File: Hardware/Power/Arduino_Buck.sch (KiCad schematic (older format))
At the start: 9 parts, among them Q3 2N7000, Q4 PJM2301PSA-S

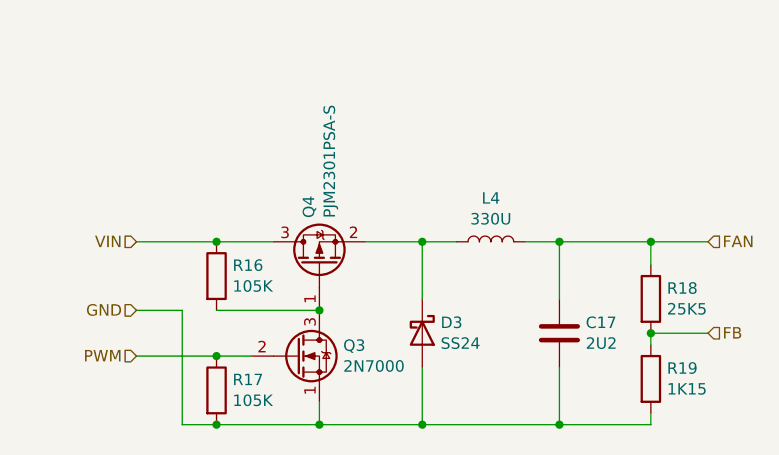
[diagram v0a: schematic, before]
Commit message: Moved MCU Power Supply to Logic Board
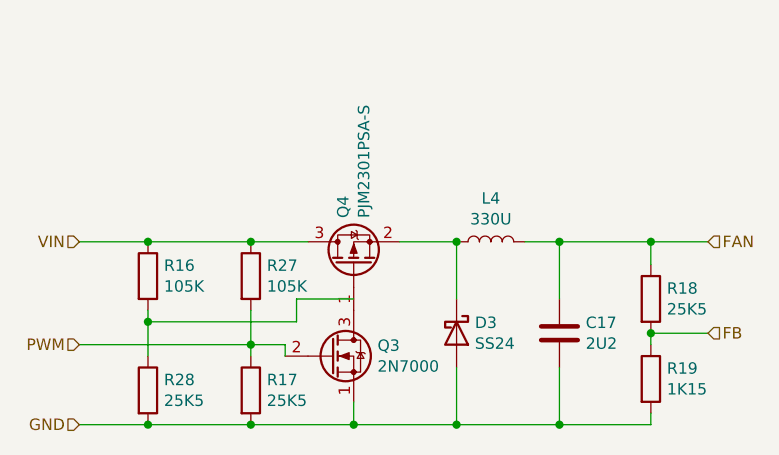
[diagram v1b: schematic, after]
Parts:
- added R27: 105K, Resistor_SMD:R_0603_1608Metric_Pad1.05x0.95mm_HandSolder, symbol Device:R
- added R28: 25K5, Resistor_SMD:R_0603_1608Metric_Pad1.05x0.95mm_HandSolder, symbol Device:R
- D3: Arrow Part Number (none) -> C181203; Mouser Part Number C181203 -> (none)
- R17: value 105K -> 25K5; Manufacturer_Part_Number RC0603FR-07105KL -> RS-05K2552FT
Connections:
- wire segments 26 -> 32
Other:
- moved on the sheet: D3, Q3, Q4, R16, R17
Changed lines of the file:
@@
 Comment4 ""
 $EndDescr
-Text HLabel 4700 3600 0    50   Input ~ 0
+Text HLabel 4450 3600 0    50   Input ~ 0
 VIN
 Text HLabel 7200 3600 2    50   Input ~ 0
 FAN
-Text HLabel 4700 3900 0    50   Input ~ 0
+Text HLabel 4450 4400 0    50   Input ~ 0
 GND
 Text HLabel 7200 4000 2    50   Input ~ 0
 FB
-Text HLabel 4700 4100 0    50   Input ~ 0
-PWM
 $Comp
 L Transistor_FET:TSM2301ACX Q4
 U 1 1 5F8E71B4
-P 5500 3700
-F 0 "Q4" H 5704 3746 50  0000 L CNN
-F 1 "PJM2301PSA-S" H 5704 3655 50  0000 L CNN
-F 2 "Package_TO_SOT_SMD:SOT-23" H 5700 3625 50  0001 L CIN
-F 3 "https://www.taiwansemi.com/products/datasheet/TSM2301A_C15.pdf" H 5500 3700 50  0001 L CNN
-F 4 "PJM2301PSA-S" H 5500 3700 50  0001 C CNN "Manufacturer_Part_Number"
-	1    5500 3700
+P 5650 3700
+F 0 "Q4" H 5854 3746 50  0000 L CNN
+F 1 "PJM2301PSA-S" H 5854 3655 50  0000 L CNN
+F 2 "Package_TO_SOT_SMD:SOT-23" H 5850 3625 50  0001 L CIN
+F 3 "https://www.taiwansemi.com/products/datasheet/TSM2301A_C15.pdf" H 5650 3700 50  0001 L CNN
+F 4 "PJM2301PSA-S" H 5650 3700 50  0001 C CNN "Manufacturer_Part_Number"
+	1    5650 3700
 	0    -1   -1   0
 $EndComp
@@
 L Device:D_Schottky D3
 U 1 1 5F8E9922
-P 5950 4000
-F 0 "D3" V 5904 4080 50  0000 L CNN
-F 1 "SS24" V 5995 4080 50  0000 L CNN
-F 2 "ArduinoLamp:D_SMA_Handsoldering_Shortened" H 5950 4000 50  0001 C CNN
-F 3 "~" H 5950 4000 50  0001 C CNN
-F 4 "C181203" H 5950 4000 50  0001 C CNN "Mouser Part Number"
-	1    5950 4000
+P 6100 4000
+F 0 "D3" V 6054 4080 50  0000 L CNN
+F 1 "SS24" V 6145 4080 50  0000 L CNN
+F 2 "ArduinoLamp:D_SMA_Handsoldering_Shortened" H 6100 4000 50  0001 C CNN
+F 3 "~" H 6100 4000 50  0001 C CNN
+F 4 "" H 6100 4000 50  0001 C CNN "Mouser Part Number"
+F 5 "C181203" H 6100 4000 50  0001 C CNN "Arrow Part Number"
+	1    6100 4000
 	0    1    1    0
 $EndComp
@@
 Wire Wire Line
 	6950 4050 6950 4000
+Wire Wire Line
+	6950 4000 7200 4000
+Connection ~ 6950 4000
+$Comp
+L Device:R R17
+U 1 1 5F8F67F8
+P 5200 4250
+F 0 "R17" H 5270 4296 50  0000 L CNN
+F 1 "25K5" H 5270 4205 50  0000 L CNN
+F 2 "Resistor_SMD:R_0603_1608Metric_Pad1.05x0.95mm_HandSolder" V 5130 4250 50  0001 C CNN
+F 3 "~" H 5200 4250 50  0001 C CNN
+F 4 "RS-05K2552FT" H 5200 4250 50  0001 C CNN "Manufacturer_Part_Number"
+	1    5200 4250
+	1    0    0    -1
+$EndComp
+Wire Wire Line
+	5650 4400 5650 4300
+Wire Wire Line
+	6550 4150 6550 4400
+Wire Wire Line
+	6950 4350 6950 4400
+Wire Wire Line
+	6950 4400 6550 4400
+Connection ~ 6550 4400
+Wire Wire Line
+	6550 3850 6550 3600
+Wire Wire Line
+	6550 3600 6950 3600
+Wire Wire Line
+	6950 3600 6950 3700
+Connection ~ 6950 3600
+Wire Wire Line
+	6950 3600 7200 3600
+Wire Wire Line
+	6400 3600 6550 3600
+Connection ~ 6550 3600
+Wire Wire Line
+	6100 3600 6100 3850
+Wire Wire Line
+	6100 4150 6100 4400
+$Comp
+L Device:R R27
+U 1 1 5FAF10C0
+P 5200 3750
+F 0 "R27" H 5270 3796 50  0000 L CNN
+F 1 "105K" H 5270 3705 50  0000 L CNN
+F 2 "Resistor_SMD:R_0603_1608Metric_Pad1.05x0.95mm_HandSolder" V 5130 3750 50  0001 C CNN
+F 3 "~" H 5200 3750 50  0001 C CNN
+F 4 "RC0603FR-07105KL" H 5200 3750 50  0001 C CNN "Manufacturer_Part_Number"
+	1    5200 3750
+	1    0    0    -1
+$EndComp
+$Comp
+L Device:R R16
+U 1 1 5F8FA0B3
+P 4750 3750
+F 0 "R16" H 4820 3796 50  0000 L CNN
+F 1 "105K" H 4820 3705 50  0000 L CNN
+F 2 "Resistor_SMD:R_0603_1608Metric_Pad1.05x0.95mm_HandSolder" V 4680 3750 50  0001 C CNN
+F 3 "~" H 4750 3750 50  0001 C CNN
+F 4 "RC0603FR-07105KL" H 4750 3750 50  0001 C CNN "Manufacturer_Part_Number"
+	1    4750 3750
+	1    0    0    -1
+$EndComp
+Connection ~ 5650 4400
+Connection ~ 6100 3600
+Wire Wire Line
+	5850 3600 6100 3600
+Connection ~ 6100 4400
+Wire Wire Line
+	6100 4400 6550 4400
+Wire Wire Line
+	5650 4400 6100 4400
 $Comp
 L Transistor_FET:2N7000 Q3
 U 1 1 5F8F3832
-P 5400 4100
-F 0 "Q3" H 5604 4146 50  0000 L CNN
-F 1 "2N7000" H 5604 4055 50  0000 L CNN
-F 2 "Package_TO_SOT_THT:TO-92_Inline" H 5600 4025 50  0001 L CIN
-F 3 "https://www.fairchildsemi.com/datasheets/2N/2N7000.pdf" H 5400 4100 50  0001 L CNN
-F 4 "2N7000" H 5400 4100 50  0001 C CNN "Manufacturer_Part_Number"
-	1    5400 4100
-	1    0    0    -1
-$EndComp
-Wire Wire Line
-	6950 4000 7200 4000
-Connection ~ 6950 4000
-Wire Wire Line
-	4700 4100 5050 4100
-$Comp
-L Device:R R17
-U 1 1 5F8F67F8
-P 5050 4250
-F 0 "R17" H 5120 4296 50  0000 L CNN
-F 1 "105K" H 5120 4205 50  0000 L CNN
-F 2 "Resistor_SMD:R_0603_1608Metric_Pad1.05x0.95mm_HandSolder" V 4980 4250 50  0001 C CNN
-F 3 "~" H 5050 4250 50  0001 C CNN
-F 4 "RC0603FR-07105KL" H 5050 4250 50  0001 C CNN "Manufacturer_Part_Number"
-	1    5050 4250
-	1    0    0    -1
-$EndComp
-Wire Wire Line
-	4700 3900 4900 3900
-$Comp
-L Device:R R16
-U 1 1 5F8FA0B3
-P 5050 3750
-F 0 "R16" H 5120 3796 50  0000 L CNN
-F 1 "105K" H 5120 3705 50  0000 L CNN
-F 2 "Resistor_SMD:R_0603_1608Metric_Pad1.05x0.95mm_HandSolder" V 4980 3750 50  0001 C CNN
-F 3 "~" H 5050 3750 50  0001 C CNN
-F 4 "RC0603FR-07105KL" H 5050 3750 50  0001 C CNN "Manufacturer_Part_Number"
-	1    5050 3750
-	1    0    0    -1
-$EndComp
-Wire Wire Line
-	4900 3900 4900 4400
-Wire Wire Line
-	4900 4400 5050 4400
-Wire Wire Line
-	5500 4400 5500 4300
-Connection ~ 5500 4400
-Wire Wire Line
-	6550 4150 6550 4400
-Wire Wire Line
-	6950 4350 6950 4400
-Wire Wire Line
-	6950 4400 6550 4400
-Connection ~ 6550 4400
-Wire Wire Line
-	4700 3600 5050 3600
-Connection ~ 5050 3600
-Wire Wire Line
-	5050 3600 5300 3600
-Wire Wire Line
-	5050 3900 5500 3900
-Connection ~ 5500 3900
-Wire Wire Line
-	6550 3850 6550 3600
-Wire Wire Line
-	6550 3600 6950 3600
-Wire Wire Line
-	6950 3600 6950 3700
-Connection ~ 6950 3600
-Wire Wire Line
-	6950 3600 7200 3600
-Connection ~ 5050 4100
-Connection ~ 5050 4400
-Wire Wire Line
-	5050 4100 5200 4100
-Wire Wire Line
-	5050 4400 5500 4400
-Wire Wire Line
-	6400 3600 6550 3600
-Connection ~ 6550 3600
-Wire Wire Line
-	5500 4400 5950 4400
-Wire Wire Line
-	5700 3600 5950 3600
-Wire Wire Line
-	5950 3600 5950 3850
-Connection ~ 5950 3600
-Wire Wire Line
-	5950 3600 6100 3600
-Wire Wire Line
-	5950 4150 5950 4400
-Connection ~ 5950 4400
-Wire Wire Line
-	5950 4400 6550 4400
+P 5550 4100
+F 0 "Q3" H 5754 4146 50  0000 L CNN
+F 1 "2N7000" H 5754 4055 50  0000 L CNN
+F 2 "Package_TO_SOT_THT:TO-92_Inline" H 5750 4025 50  0001 L CIN
+F 3 "https://www.fairchildsemi.com/datasheets/2N/2N7000.pdf" H 5550 4100 50  0001 L CNN
+F 4 "2N7000" H 5550 4100 50  0001 C CNN "Manufacturer_Part_Number"
+	1    5550 4100
+	1    0    0    -1
+$EndComp
+Connection ~ 5200 3600
+Wire Wire Line
+	5200 4400 5650 4400
+Wire Wire Line
+	4450 3600 4750 3600
+Connection ~ 4750 3600
+Wire Wire Line
+	4750 3600 5200 3600
+Wire Wire Line
+	4750 3900 4750 3950
+Wire Wire Line
+	5200 3600 5450 3600
+Wire Wire Line
+	5650 3850 5400 3850
+Wire Wire Line
+	5400 3850 5400 3950
+Wire Wire Line
+	5400 3950 4750 3950
+Connection ~ 4750 3950
+Wire Wire Line
+	4750 3950 4750 4100
+Wire Wire Line
+	4450 4050 5200 4050
+Text HLabel 4450 4050 0    50   Input ~ 0
+PWM
+Connection ~ 5200 4050
+Wire Wire Line
+	5200 4050 5200 4100
+Wire Wire Line
+	5200 3900 5200 4050
+Wire Wire Line
+	5200 4050 5350 4050
+Wire Wire Line
+	5350 4050 5350 4100
+$Comp
+L Device:R R28
+U 1 1 5FB23D33
+P 4750 4250
+F 0 "R28" H 4820 4296 50  0000 L CNN
+F 1 "25K5" H 4820 4205 50  0000 L CNN
+F 2 "Resistor_SMD:R_0603_1608Metric_Pad1.05x0.95mm_HandSolder" V 4680 4250 50  0001 C CNN
+F 3 "~" H 4750 4250 50  0001 C CNN
+F 4 "RS-05K2552FT" H 4750 4250 50  0001 C CNN "Manufacturer_Part_Number"
+	1    4750 4250
+	1    0    0    -1
+$EndComp
+Wire Wire Line
+	4450 4400 4750 4400
+Wire Wire Line
+	4750 4400 5200 4400
+Connection ~ 4750 4400
+Connection ~ 5200 4400
 $EndSCHEMATC

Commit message: Removed Logic Board PSU from Power Board
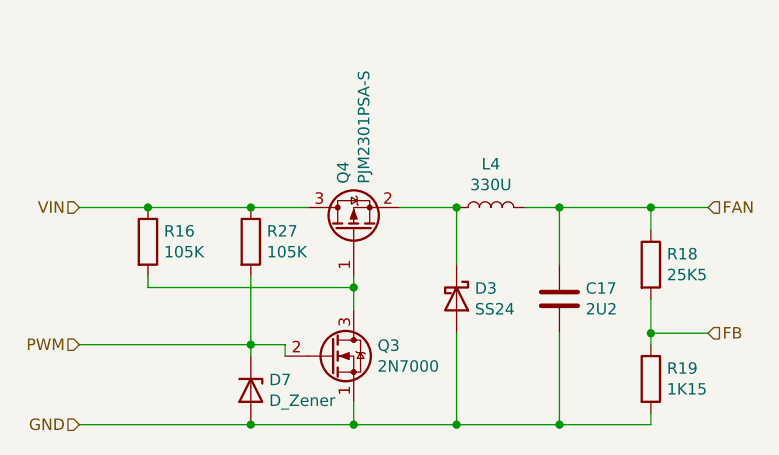
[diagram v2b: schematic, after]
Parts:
- removed R17, R28: 25K5, Resistor_SMD:R_0603_1608Metric_Pad1.05x0.95mm_HandSolder, symbol Device:R
- added D7: D_Zener, Diode_SMD:D_SOD-323_HandSoldering, symbol Device:D_Zener
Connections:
- wire segments 32 -> 31
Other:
- moved on the sheet: C17, D3, L4, Q4, R16, R18, R27
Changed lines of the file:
@@
 Comment4 ""
 $EndDescr
-Text HLabel 4450 3600 0    50   Input ~ 0
+Text HLabel 4450 3450 0    50   Input ~ 0
 VIN
-Text HLabel 7200 3600 2    50   Input ~ 0
+Text HLabel 7200 3450 2    50   Input ~ 0
 FAN
 Text HLabel 4450 4400 0    50   Input ~ 0
@@
 FB
 $Comp
-L Transistor_FET:TSM2301ACX Q4
-U 1 1 5F8E71B4
-P 5650 3700
-F 0 "Q4" H 5854 3746 50  0000 L CNN
-F 1 "PJM2301PSA-S" H 5854 3655 50  0000 L CNN
-F 2 "Package_TO_SOT_SMD:SOT-23" H 5850 3625 50  0001 L CIN
-F 3 "https://www.taiwansemi.com/products/datasheet/TSM2301A_C15.pdf" H 5650 3700 50  0001 L CNN
-F 4 "PJM2301PSA-S" H 5650 3700 50  0001 C CNN "Manufacturer_Part_Number"
-	1    5650 3700
-	0    -1   -1   0
-$EndComp
-$Comp
 L Device:L L4
 U 1 1 5F8E9295
-P 6250 3600
-F 0 "L4" V 6440 3600 50  0000 C CNN
-F 1 "330U" V 6349 3600 50  0000 C CNN
-F 2 "ArduinoLamp:SLD10" H 6250 3600 50  0001 C CNN
-F 3 "~" H 6250 3600 50  0001 C CNN
-F 4 "SLD10D40S331MTT" H 6250 3600 50  0001 C CNN "Manufacturer_Part_Number"
-	1    6250 3600
+P 6250 3450
+F 0 "L4" V 6440 3450 50  0000 C CNN
+F 1 "330U" V 6349 3450 50  0000 C CNN
+F 2 "ArduinoLamp:SLD10" H 6250 3450 50  0001 C CNN
+F 3 "~" H 6250 3450 50  0001 C CNN
+F 4 "SLD10D40S331MTT" H 6250 3450 50  0001 C CNN "Manufacturer_Part_Number"
+	1    6250 3450
 	0    -1   -1   0
 $EndComp
@@
 L Device:D_Schottky D3
 U 1 1 5F8E9922
-P 6100 4000
-F 0 "D3" V 6054 4080 50  0000 L CNN
-F 1 "SS24" V 6145 4080 50  0000 L CNN
-F 2 "ArduinoLamp:D_SMA_Handsoldering_Shortened" H 6100 4000 50  0001 C CNN
-F 3 "~" H 6100 4000 50  0001 C CNN
-F 4 "" H 6100 4000 50  0001 C CNN "Mouser Part Number"
-F 5 "C181203" H 6100 4000 50  0001 C CNN "Arrow Part Number"
-	1    6100 4000
+P 6100 3850
+F 0 "D3" V 6054 3930 50  0000 L CNN
+F 1 "SS24" V 6145 3930 50  0000 L CNN
+F 2 "ArduinoLamp:D_SMA_Handsoldering_Shortened" H 6100 3850 50  0001 C CNN
+F 3 "~" H 6100 3850 50  0001 C CNN
+F 4 "" H 6100 3850 50  0001 C CNN "Mouser Part Number"
+F 5 "C181203" H 6100 3850 50  0001 C CNN "Arrow Part Number"
+	1    6100 3850
 	0    1    1    0
 $EndComp
@@
 L Device:C C17
 U 1 1 5F8EC349
-P 6550 4000
-F 0 "C17" H 6665 4046 50  0000 L CNN
-F 1 "2U2" H 6665 3955 50  0000 L CNN
-F 2 "Capacitor_SMD:C_0805_2012Metric_Pad1.15x1.40mm_HandSolder" H 6588 3850 50  0001 C CNN
-F 3 "~" H 6550 4000 50  0001 C CNN
-F 4 "C0805X5R225K500NT" H 6550 4000 50  0001 C CNN "Manufacturer_Part_Number"
-	1    6550 4000
+P 6550 3850
+F 0 "C17" H 6665 3896 50  0000 L CNN
+F 1 "2U2" H 6665 3805 50  0000 L CNN
+F 2 "Capacitor_SMD:C_0805_2012Metric_Pad1.15x1.40mm_HandSolder" H 6588 3700 50  0001 C CNN
+F 3 "~" H 6550 3850 50  0001 C CNN
+F 4 "C0805X5R225K500NT" H 6550 3850 50  0001 C CNN "Manufacturer_Part_Number"
+	1    6550 3850
 	1    0    0    -1
 $EndComp
@@
 L Device:R R18
 U 1 1 5F8ECD7F
-P 6950 3850
-F 0 "R18" H 7020 3896 50  0000 L CNN
-F 1 "25K5" H 7020 3805 50  0000 L CNN
-F 2 "Resistor_SMD:R_0603_1608Metric_Pad1.05x0.95mm_HandSolder" V 6880 3850 50  0001 C CNN
-F 3 "~" H 6950 3850 50  0001 C CNN
-F 4 "RS-05K2552FT" H 6950 3850 50  0001 C CNN "Manufacturer_Part_Number"
-	1    6950 3850
+P 6950 3700
+F 0 "R18" H 7020 3746 50  0000 L CNN
+F 1 "25K5" H 7020 3655 50  0000 L CNN
+F 2 "Resistor_SMD:R_0603_1608Metric_Pad1.05x0.95mm_HandSolder" V 6880 3700 50  0001 C CNN
+F 3 "~" H 6950 3700 50  0001 C CNN
+F 4 "RS-05K2552FT" H 6950 3700 50  0001 C CNN "Manufacturer_Part_Number"
+	1    6950 3700
 	1    0    0    -1
 $EndComp
@@
 Wire Wire Line
 	6950 4000 7200 4000
-Connection ~ 6950 4000
-$Comp
-L Device:R R17
-U 1 1 5F8F67F8
-P 5200 4250
-F 0 "R17" H 5270 4296 50  0000 L CNN
-F 1 "25K5" H 5270 4205 50  0000 L CNN
-F 2 "Resistor_SMD:R_0603_1608Metric_Pad1.05x0.95mm_HandSolder" V 5130 4250 50  0001 C CNN
-F 3 "~" H 5200 4250 50  0001 C CNN
-F 4 "RS-05K2552FT" H 5200 4250 50  0001 C CNN "Manufacturer_Part_Number"
-	1    5200 4250
-	1    0    0    -1
-$EndComp
 Wire Wire Line
 	5650 4400 5650 4300
-Wire Wire Line
-	6550 4150 6550 4400
 Wire Wire Line
 	6950 4350 6950 4400
@@
 Connection ~ 6550 4400
 Wire Wire Line
-	6550 3850 6550 3600
-Wire Wire Line
-	6550 3600 6950 3600
-Wire Wire Line
-	6950 3600 6950 3700
-Connection ~ 6950 3600
-Wire Wire Line
-	6950 3600 7200 3600
-Wire Wire Line
-	6400 3600 6550 3600
-Connection ~ 6550 3600
-Wire Wire Line
-	6100 3600 6100 3850
-Wire Wire Line
-	6100 4150 6100 4400
+	6550 3700 6550 3450
+Wire Wire Line
+	6550 3450 6950 3450
+Wire Wire Line
+	6950 3450 6950 3550
+Connection ~ 6950 3450
+Wire Wire Line
+	6950 3450 7200 3450
+Wire Wire Line
+	6400 3450 6550 3450
+Connection ~ 6550 3450
+Wire Wire Line
+	6100 3450 6100 3700
 $Comp
 L Device:R R27
 U 1 1 5FAF10C0
-P 5200 3750
-F 0 "R27" H 5270 3796 50  0000 L CNN
-F 1 "105K" H 5270 3705 50  0000 L CNN
-F 2 "Resistor_SMD:R_0603_1608Metric_Pad1.05x0.95mm_HandSolder" V 5130 3750 50  0001 C CNN
-F 3 "~" H 5200 3750 50  0001 C CNN
-F 4 "RC0603FR-07105KL" H 5200 3750 50  0001 C CNN "Manufacturer_Part_Number"
-	1    5200 3750
+P 5200 3600
+F 0 "R27" H 5270 3646 50  0000 L CNN
+F 1 "105K" H 5270 3555 50  0000 L CNN
+F 2 "Resistor_SMD:R_0603_1608Metric_Pad1.05x0.95mm_HandSolder" V 5130 3600 50  0001 C CNN
+F 3 "~" H 5200 3600 50  0001 C CNN
+F 4 "RC0603FR-07105KL" H 5200 3600 50  0001 C CNN "Manufacturer_Part_Number"
+	1    5200 3600
 	1    0    0    -1
 $EndComp
@@
 L Device:R R16
 U 1 1 5F8FA0B3
-P 4750 3750
-F 0 "R16" H 4820 3796 50  0000 L CNN
-F 1 "105K" H 4820 3705 50  0000 L CNN
-F 2 "Resistor_SMD:R_0603_1608Metric_Pad1.05x0.95mm_HandSolder" V 4680 3750 50  0001 C CNN
-F 3 "~" H 4750 3750 50  0001 C CNN
-F 4 "RC0603FR-07105KL" H 4750 3750 50  0001 C CNN "Manufacturer_Part_Number"
-	1    4750 3750
+P 4750 3600
+F 0 "R16" H 4820 3646 50  0000 L CNN
+F 1 "105K" H 4820 3555 50  0000 L CNN
+F 2 "Resistor_SMD:R_0603_1608Metric_Pad1.05x0.95mm_HandSolder" V 4680 3600 50  0001 C CNN
+F 3 "~" H 4750 3600 50  0001 C CNN
+F 4 "RC0603FR-07105KL" H 4750 3600 50  0001 C CNN "Manufacturer_Part_Number"
+	1    4750 3600
 	1    0    0    -1
 $EndComp
 Connection ~ 5650 4400
-Connection ~ 6100 3600
-Wire Wire Line
-	5850 3600 6100 3600
+Connection ~ 6100 3450
+Wire Wire Line
+	5850 3450 6100 3450
 Connection ~ 6100 4400
 Wire Wire Line
@@
 	1    0    0    -1
 $EndComp
-Connection ~ 5200 3600
-Wire Wire Line
-	5200 4400 5650 4400
-Wire Wire Line
-	4450 3600 4750 3600
-Connection ~ 4750 3600
-Wire Wire Line
-	4750 3600 5200 3600
-Wire Wire Line
-	4750 3900 4750 3950
-Wire Wire Line
-	5200 3600 5450 3600
-Wire Wire Line
-	5650 3850 5400 3850
-Wire Wire Line
-	5400 3850 5400 3950
-Wire Wire Line
-	5400 3950 4750 3950
-Connection ~ 4750 3950
-Wire Wire Line
-	4750 3950 4750 4100
+Connection ~ 5200 3450
+Wire Wire Line
+	4450 3450 4750 3450
+Connection ~ 4750 3450
+Wire Wire Line
+	4750 3450 5200 3450
+Wire Wire Line
+	4750 3750 4750 3800
+Wire Wire Line
+	5200 3450 5450 3450
 Wire Wire Line
 	4450 4050 5200 4050
@@
 	5200 4050 5200 4100
 Wire Wire Line
-	5200 3900 5200 4050
-Wire Wire Line
 	5200 4050 5350 4050
 Wire Wire Line
 	5350 4050 5350 4100
 $Comp
-L Device:R R28
-U 1 1 5FB23D33
-P 4750 4250
-F 0 "R28" H 4820 4296 50  0000 L CNN
-F 1 "25K5" H 4820 4205 50  0000 L CNN
-F 2 "Resistor_SMD:R_0603_1608Metric_Pad1.05x0.95mm_HandSolder" V 4680 4250 50  0001 C CNN
-F 3 "~" H 4750 4250 50  0001 C CNN
-F 4 "RS-05K2552FT" H 4750 4250 50  0001 C CNN "Manufacturer_Part_Number"
-	1    4750 4250
-	1    0    0    -1
-$EndComp
-Wire Wire Line
-	4450 4400 4750 4400
-Wire Wire Line
-	4750 4400 5200 4400
-Connection ~ 4750 4400
+L Transistor_FET:TSM2301ACX Q4
+U 1 1 5F8E71B4
+P 5650 3550
+F 0 "Q4" H 5854 3596 50  0000 L CNN
+F 1 "PJM2301PSA-S" H 5854 3505 50  0000 L CNN
+F 2 "Package_TO_SOT_SMD:SOT-23" H 5850 3475 50  0001 L CIN
+F 3 "https://www.taiwansemi.com/products/datasheet/TSM2301A_C15.pdf" H 5650 3550 50  0001 L CNN
+F 4 "PJM2301PSA-S" H 5650 3550 50  0001 C CNN "Manufacturer_Part_Number"
+	1    5650 3550
+	0    -1   -1   0
+$EndComp
+Wire Wire Line
+	5200 3750 5200 4050
+Wire Wire Line
+	6100 4000 6100 4400
+Wire Wire Line
+	6550 4000 6550 4400
+Wire Wire Line
+	5650 3800 5650 3750
+Wire Wire Line
+	4750 3800 5650 3800
+Wire Wire Line
+	5650 3900 5650 3800
+Connection ~ 5650 3800
+Wire Wire Line
+	6950 3850 6950 4000
+Connection ~ 6950 4000
+Wire Wire Line
+	4450 4400 5200 4400
+$Comp
+L Device:D_Zener D7
+U 1 1 5FB97005
+P 5200 4250
+F 0 "D7" V 5154 4330 50  0000 L CNN
+F 1 "D_Zener" V 5245 4330 50  0000 L CNN
+F 2 "Diode_SMD:D_SOD-323_HandSoldering" H 5200 4250 50  0001 C CNN
+F 3 "~" H 5200 4250 50  0001 C CNN
+	1    5200 4250
+	0    1    1    0
+$EndComp
 Connection ~ 5200 4400
+Wire Wire Line
+	5200 4400 5650 4400
 $EndSCHEMATC
